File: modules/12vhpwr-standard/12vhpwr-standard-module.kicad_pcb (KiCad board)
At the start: 4 copper layers, 58 x 80 mm, 71 parts, among them J1 TO-HUB, J3 12V-2x6 IN, J4 12V-2x6 OUT pigtail, J5 USB-C 2.0, SW1 BOOT, SW2 RESET, U1 ESP32-S3-MINI-1-N4R2, U10 INA240A3, U11 INA240A3, U12 INA240A3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

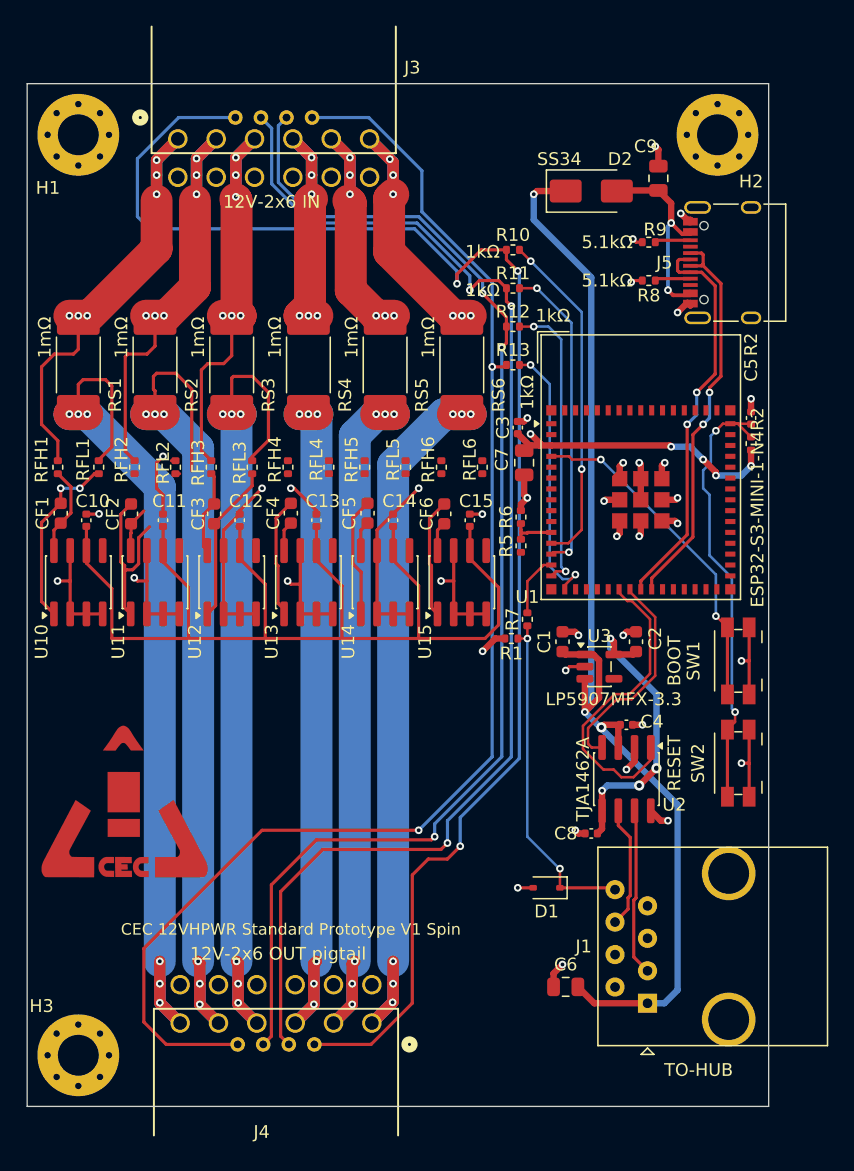
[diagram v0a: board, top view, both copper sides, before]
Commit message: 12VHPWR Main Routing Complete.
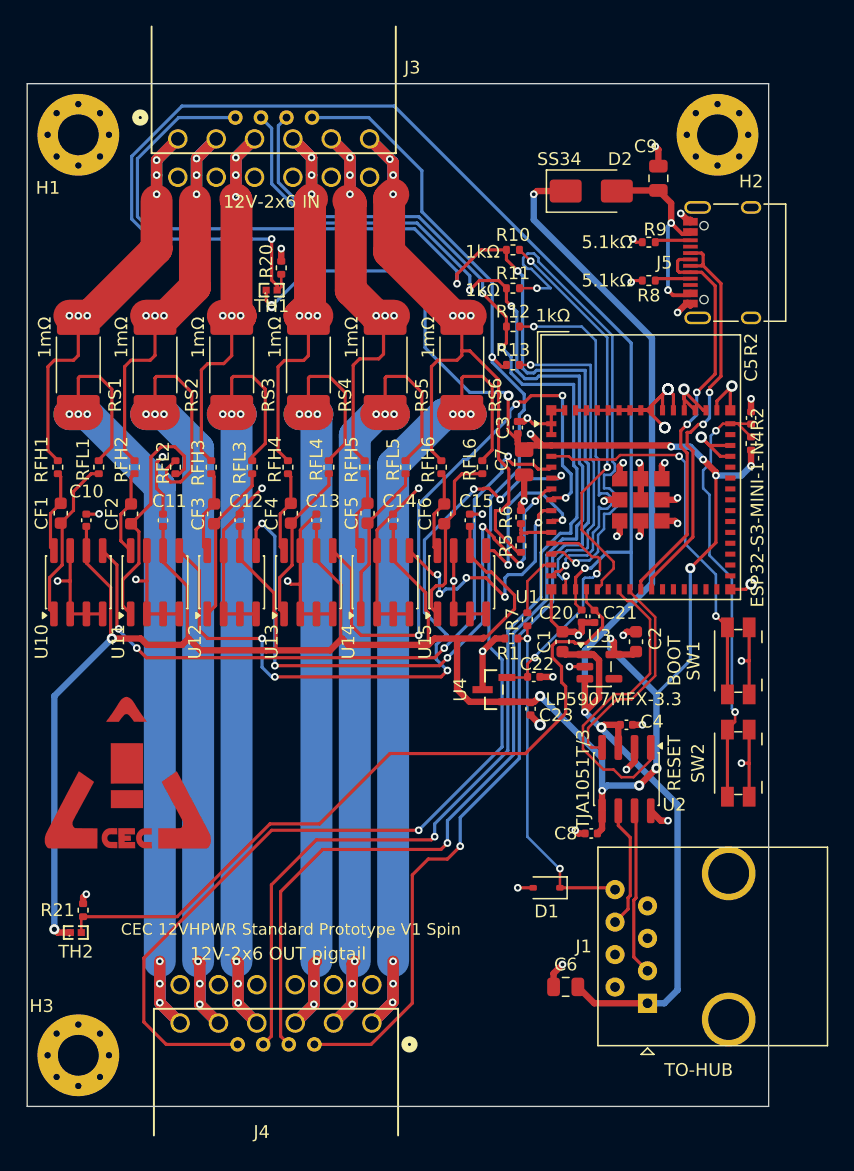
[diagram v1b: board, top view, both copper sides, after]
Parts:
- added C20: 100nF, cec-Capacitor_SMD:C_0402_1005Metric, F.Cu at (156.2, 100.0)
- added C21: 100nF, cec-Capacitor_SMD:C_0402_1005Metric, F.Cu at (157.2, 100.0)
- added C22: 100nF, cec-Capacitor_SMD:C_0402_1005Metric, F.Cu at (152.5, 104.8)
- added C23: 100nF, cec-Capacitor_SMD:C_0402_1005Metric, F.Cu at (152.2, 107.2)
- added R20: 10kΩ, cec-Resistor_SMD:R_0402_1005Metric, F.Cu at (132.8, 72.8)
- added R21: 10kΩ, cec-Resistor_SMD:R_0402_1005Metric, F.Cu at (117.2, 123.0)
- added TH1: NTC 10k, cec-Resistor_SMD:NTC_0402_1005Metric, F.Cu at (132.0, 74.5)
- added TH2: NTC 10k, cec-Resistor_SMD:NTC_0402_1005Metric, F.Cu at (116.7, 124.8)
- added U4: REF3030, cec-Package_TO_SOT_SMD:REF3030_DBZ3, F.Cu at (149.4, 105.8)
- U2: value TJA1462A -> TJA1051T/3
- moved LOGO1 2.26 mm to (120.8, 112.2)
- turned CF1 to -90 degrees
- turned CF2 to -90 degrees
- turned CF4 to -90 degrees
- turned CF5 to -90 degrees
- turned CF6 to -90 degrees
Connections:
- R5 pad 1: /SENSEP1_HI -> /SENSEP6_HI
- U1 pad 12: /SB_SENSE0_GPIO -> /VREF
- U1 pad 17: unconnected-(U1-IO13-Pad17) -> /TEMP1
- U1 pad 18: unconnected-(U1-IO14-Pad18) -> /TEMP2
- U1 pad 19: unconnected-(U1-IO15-Pad19) -> /SB_SENSE0_GPIO
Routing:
- net +3V3: track 132.3 -> 236.7 mm, vias 9 -> 15
- net /TEMP1: track 0.00 -> 97.6 mm, vias 0 -> 2
- net /TEMP2: track 0.00 -> 59.5 mm
- net GND: track 121.1 -> 177.8 mm, vias 38 -> 50
- net /ISENSEP2: track 0.00 -> 55.6 mm, vias 0 -> 6
- net /ISENSEP1: track 0.00 -> 54.5 mm, vias 0 -> 4
- net /ISENSEP3: track 0.00 -> 50.4 mm, vias 0 -> 6
- net /ISENSEP4: track 0.00 -> 47.0 mm, vias 0 -> 4
- net /SENSEP6_HI: track 24.0 -> 55.9 mm
- net /ISENSEP5: track 0.00 -> 20.1 mm, vias 0 -> 5
- net /VREF: track 0.00 -> 17.9 mm, vias 0 -> 2
- net /SB_SENSE1_GPIO: track 24.7 -> 40.1 mm
- net /ISENSEP6: track 0.00 -> 13.6 mm, vias 0 -> 2
- net /SENSEP5_HI: track 21.7 -> 34.4 mm
- net /SENSEP4_HI: track 20.8 -> 33.4 mm
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
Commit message: PCB Update.
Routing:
- net /TEMP1: track 97.6 -> 94.7 mm
- net /SENSEP5_HI: track 34.4 -> 36.5 mm, vias 6 -> 10
- net /SENSEP2_HI: track 34.6 -> 36.0 mm, vias 6 -> 10
- net /SENSEP1_HI: track 35.7 -> 37.1 mm, vias 6 -> 10
- net /SENSEP6_HI: track 55.9 -> 57.3 mm, vias 6 -> 10
- net /SENSEP4_HI: track 33.4 -> 34.8 mm, vias 6 -> 10
- net /SENSEP3_HI: track 33.5 -> 34.9 mm, vias 6 -> 10
- net /SENSEP6_LO: vias 6 -> 10
- net /SENSEP5_LO: vias 6 -> 10
- net /SENSEP4_LO: vias 6 -> 10
- net /SENSEP3_LO: vias 6 -> 10
- net /SENSEP2_LO: vias 6 -> 10
- net /SENSEP1_LO: vias 6 -> 10

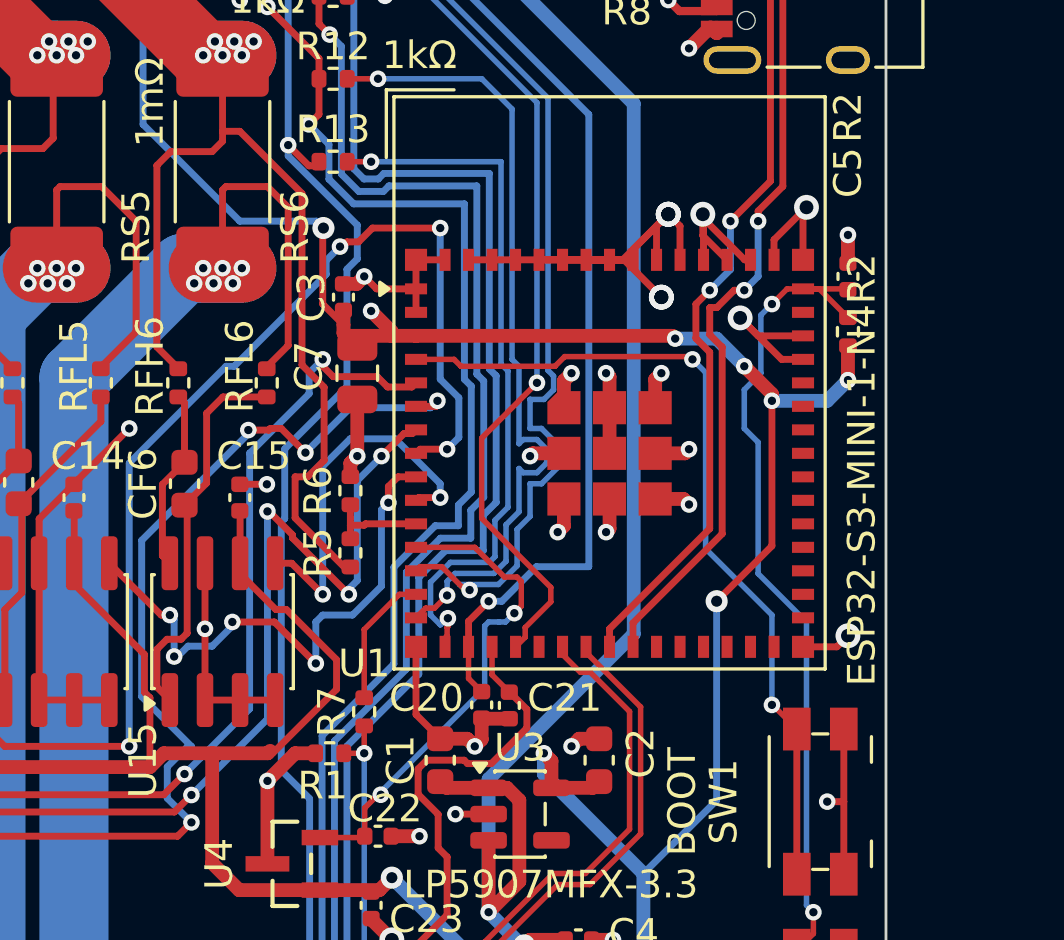
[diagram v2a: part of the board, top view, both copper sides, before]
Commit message: Added more thermal vias, fixed more DRC.
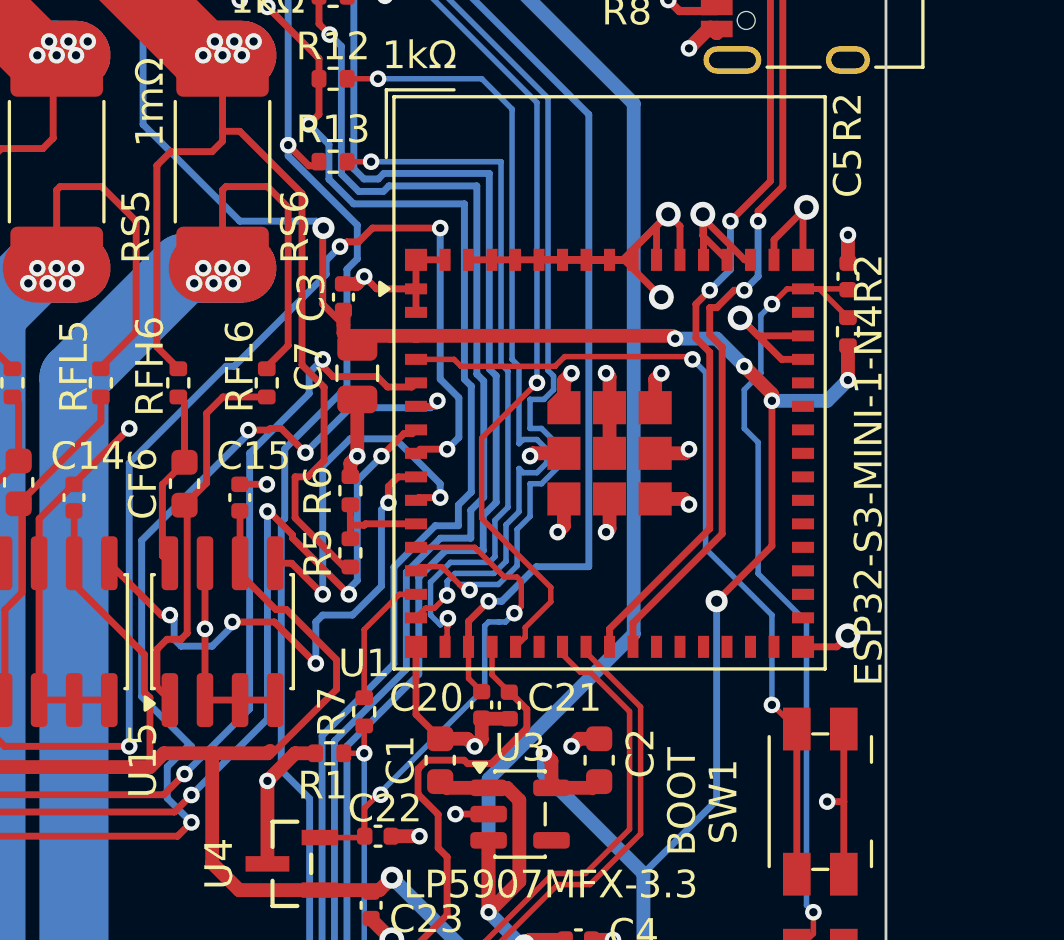
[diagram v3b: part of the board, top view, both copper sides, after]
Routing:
- net +3V3: track 236.7 -> 235.5 mm, vias 15 -> 14
- net /ISENSEP5: track 20.1 -> 19.5 mm, vias 5 -> 4
- net GND: vias 50 -> 47
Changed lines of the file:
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@@
 		)
 		(property "Value" "ESP32-S3-MINI-1-N4R2"
-			(at 9.125 3.15 90)
+			(at 9.375 3.15 90)
 			(unlocked yes)
 			(layer "F.SilkS")
@@
 	)
 	(via
-		(at 163 82.25)
-		(size 0.9)
-		(drill 0.5)
-		(layers "F.Cu" "B.Cu")
-		(net "GND")
-	)
-	(via
 		(at 132.75 71.25)
 		(size 0.6)
@@
 	)
 	(via
-		(at 162.75 85.25)
-		(size 0.9)
-		(drill 0.5)
-		(layers "F.Cu" "B.Cu")
-		(net "GND")
-	)
-	(via
 		(at 159.5 88)
 		(size 0.6)
@@
 	)
 	(via
-		(at 163 82.25)
-		(size 0.9)
-		(drill 0.5)
-		(layers "F.Cu" "B.Cu")
-		(net "GND")
-	)
-	(via
 		(at 155.3 103.95)
 		(size 0.6)
@@
 	)
 	(segment
-		(start 153 86.5)
-		(end 152.25 85.75)
-		(width 0.5)
-		(layer "F.Cu")
-		(net "+3V3")
-	)
-	(segment
 		(start 131.575 102.675)
 		(end 136.575 102.675)
@@
 	)
 	(segment
-		(start 153 86.65)
-		(end 153 86.5)
-		(width 0.5)
-		(layer "F.Cu")
-		(net "+3V3")
-	)
-	(segment
 		(start 158.775 103)
 		(end 160.275 103)
@@
 	)
 	(via
-		(at 152.25 85.75)
-		(size 0.6)
-		(drill 0.3)
-		(layers "F.Cu" "B.Cu")
-		(net "+3V3")
-	)
-	(via
 		(at 115 124.5)
 		(size 0.8)
@@
 	)
 	(via
-		(at 145.125 98.25)
-		(size 0.6)
-		(drill 0.3)
-		(layers "F.Cu" "B.Cu")
-		(net "/ISENSEP5")
-	)
-	(via
 		(at 150.25 98.5)
 		(size 0.6)
@@
 	)
 	(segment
-		(start 146.498884 97.875)
-		(end 147.23 97.143884)
-		(width 0.25)
-		(layer "B.Cu")
-		(net "/ISENSEP5")
-	)
-	(segment
-		(start 147.23 97.143884)
-		(end 147.23 97)
+		(start 144.97 96.75)
+		(end 145.125 96.905)
 		(width 0.25)
 		(layer "B.Cu")
@@
 	)
 	(segment
-		(start 145.125 96.905)
-		(end 144.97 96.75)
+		(start 152.625 92.937381)
+		(end 152.625 95.703894)
 		(width 0.25)
 		(layer "B.Cu")
@@
 	)
 	(segment
-		(start 152.625 92.937381)
-		(end 152.625 95.703894)
+		(start 145.375 97.875)
+		(end 146.498884 97.875)
 		(width 0.25)
 		(layer "B.Cu")
@@
 	)
 	(segment
-		(start 150.25 97)
-		(end 150.25 98.5)
+		(start 145.125 97.625)
+		(end 145.375 97.875)
 		(width 0.25)
 		(layer "B.Cu")
@@
 	)
 	(segment
-		(start 145.25 98.25)
-		(end 145.625 97.875)
+		(start 147.23 97.143884)
+		(end 147.23 97)
 		(width 0.25)
 		(layer "B.Cu")
@@
 	)
 	(segment
-		(start 145.125 98.25)
-		(end 145.25 98.25)
+		(start 150.25 97)
+		(end 150.25 98.5)
 		(width 0.25)
 		(layer "B.Cu")
@@
 	)
 	(segment
-		(start 145.125 98.25)
-		(end 145.125 96.905)
+		(start 146.498884 97.875)
+		(end 147.23 97.143884)
 		(width 0.25)
 		(layer "B.Cu")
@@
 	)
 	(segment
-		(start 145.625 97.875)
-		(end 146.498884 97.875)
+		(start 145.125 96.905)
+		(end 145.125 97.625)
 		(width 0.25)
 		(layer "B.Cu")

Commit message: Minor PCB Edits.
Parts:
- moved LOGO1 1.60 mm to (122.0, 111.2), turned to 0 degrees

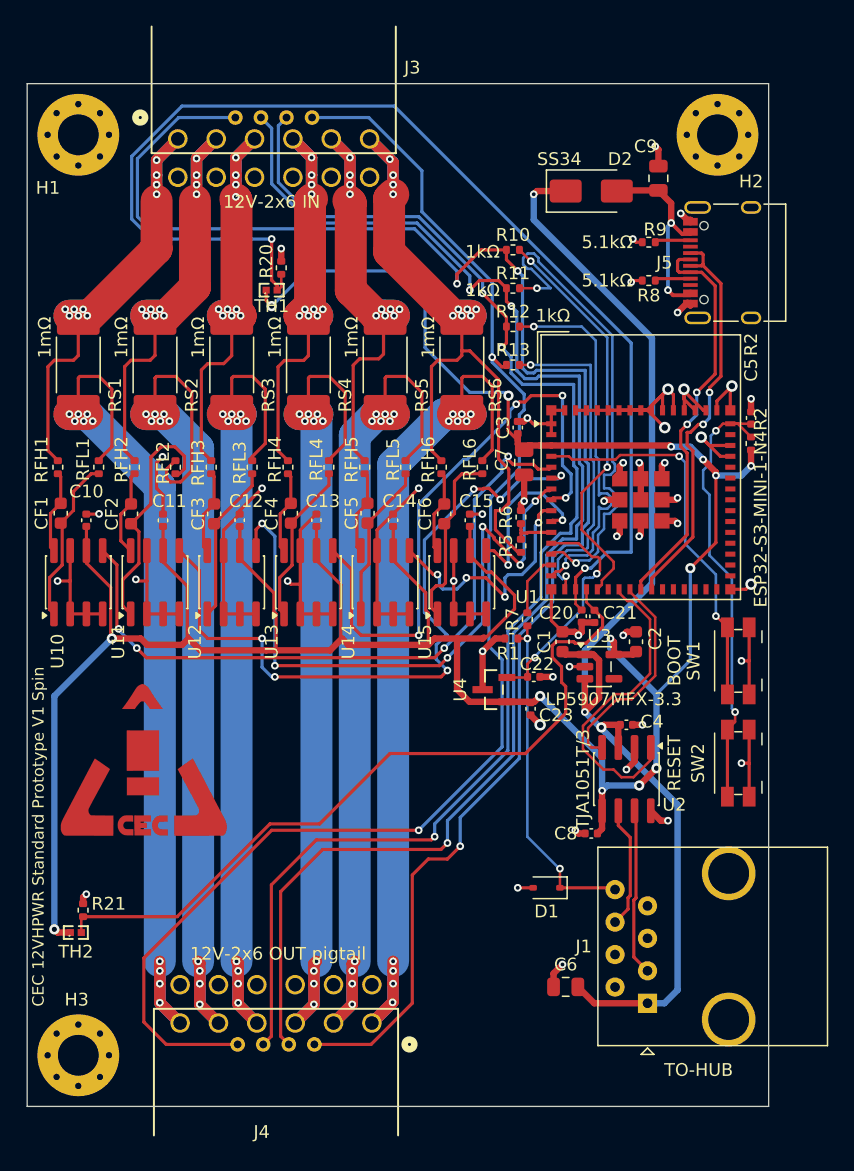
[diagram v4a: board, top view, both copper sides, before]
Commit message: Added ground via stitching, ring of ground vias, updated PCB.
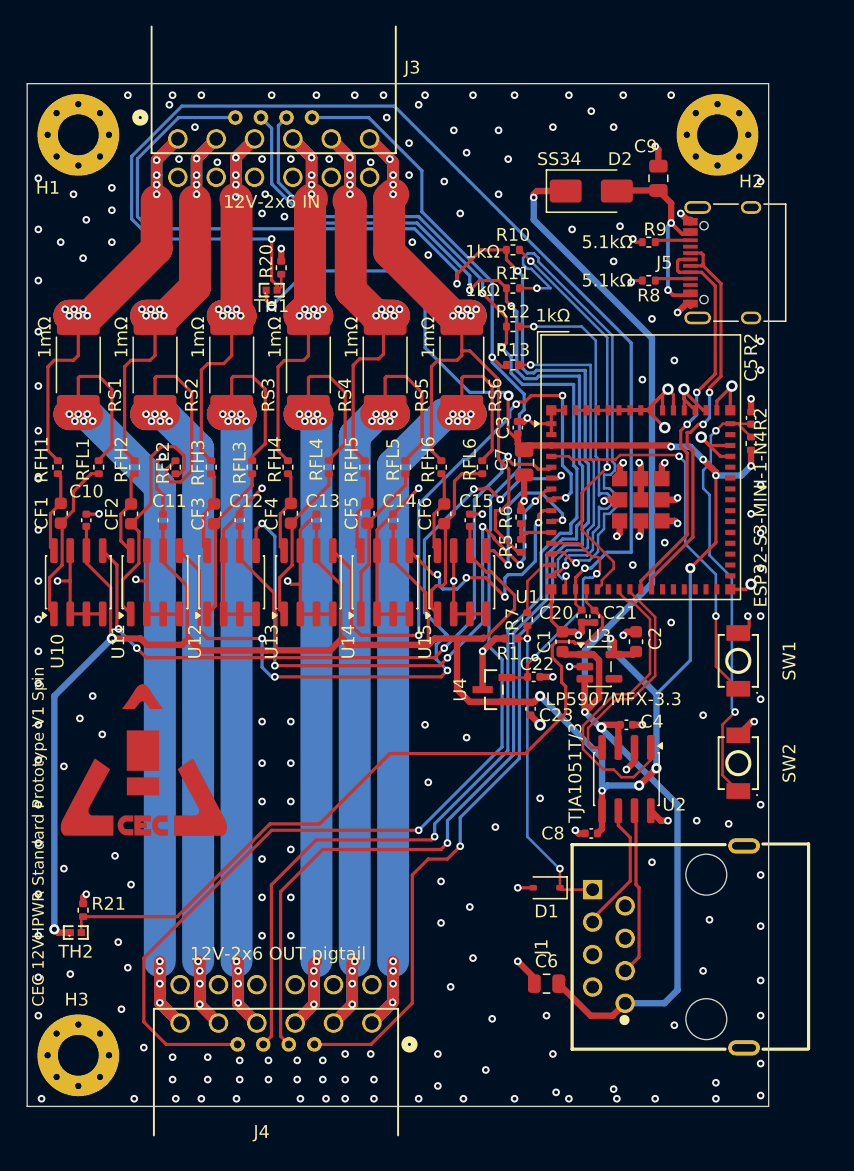
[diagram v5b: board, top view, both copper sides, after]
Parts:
- D1: value PESD5V0S1UL -> PESD5V0S1BA
- J1: footprint cec-Connector_RJ:RJ45_Amphenol_54602-x08_Horizontal -> cec:RJ45_FTP_Shielded_Horizontal
- SW1, SW2: footprint cec-Button_Switch_SMD:Panasonic_EVQPUJ_EVQPUA -> cec-Button_Switch_SMD:TS-1088-AR02016
- moved J1 1.75 mm to (159.7, 130.3)
- moved C6 1.52 mm to (153.5, 128.8)
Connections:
- J1 pad SH1: unconnected-(J1-SHIELD-PadSH1) -> GND
- J1 pad SH2: unconnected-(J1-SHIELD-PadSH2) -> GND
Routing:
- net GND: track 177.8 -> 169.0 mm, vias 47 -> 221
- net +5VSB: track 96.3 -> 99.1 mm
- net /DETECT: track 26.7 -> 24.9 mm
- net unconnected-(J1-RSVD-Pad7): track 0.00 -> 0.89 mm
- net /CAN_L: track 9.59 -> 10.3 mm

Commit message: Re-routing.
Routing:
- net /SB_SENSE0: track 127.6 -> 72.4 mm
- net /SB_SENSE1: track 109.1 -> 56.9 mm
- net /SB_PWR_STABLE: track 105.9 -> 57.7 mm
- net /SB_CBL_PRES: track 109.7 -> 67.4 mm
- net /SB_SENSE1_GPIO: track 40.1 -> 3.71 mm
- net /SB_SENSE0_GPIO: track 31.8 -> 1.25 mm, vias 2 -> 1
- net /SB_PWR_STABLE_GPIO: track 29.5 -> 2.57 mm
- net /SB_CBL_PRES_GPIO: track 26.0 -> 1.94 mm
- net /ISENSEP4: track 47.0 -> 31.9 mm, vias 4 -> 2
- net /INNP1: track 13.2 -> 0.19 mm
- net +3V3: track 235.5 -> 247.5 mm, vias 14 -> 22
- net /ISENSEP2: track 55.6 -> 48.1 mm, vias 6 -> 2
- net +5VSB: track 99.1 -> 106.5 mm
- net /INPP1: track 6.55 -> 0.00 mm
- net /ISENSEP1: track 54.5 -> 57.8 mm, vias 4 -> 2
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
